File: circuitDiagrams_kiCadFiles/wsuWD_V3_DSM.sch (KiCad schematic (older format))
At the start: 54 parts

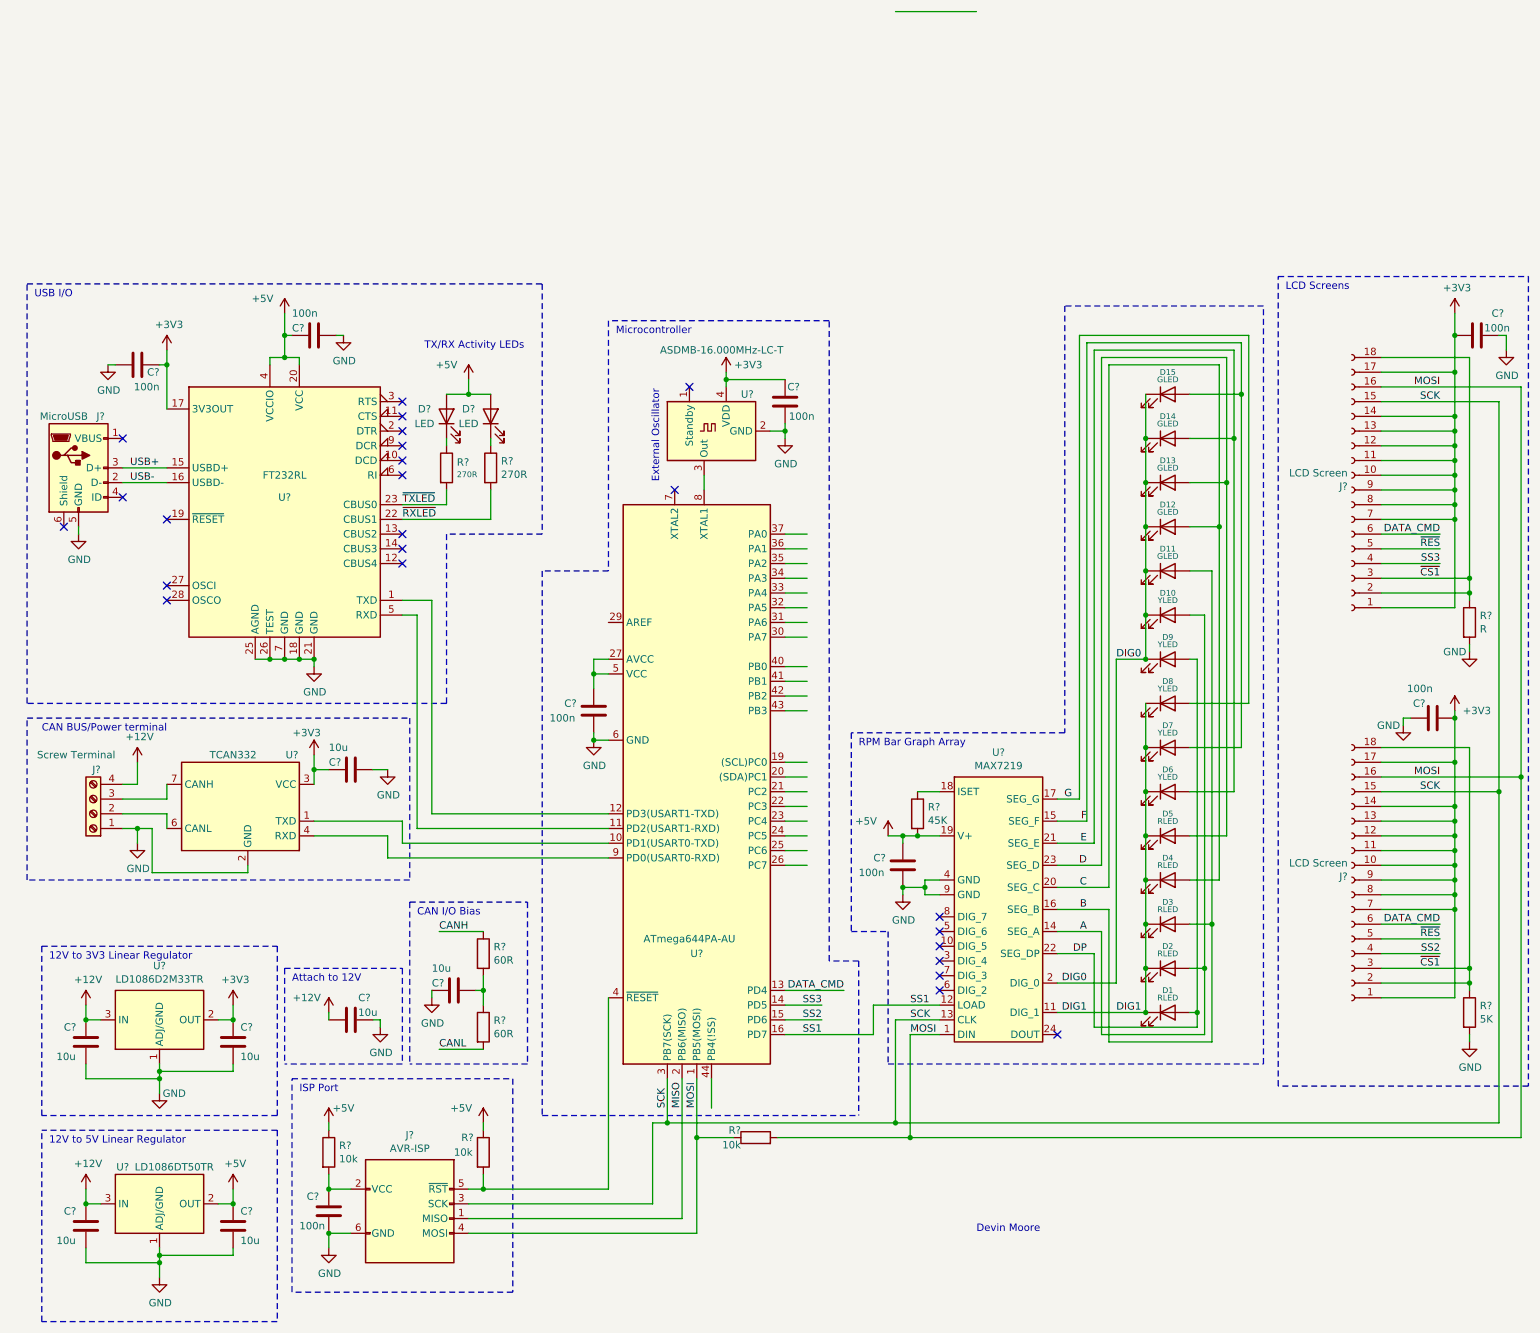
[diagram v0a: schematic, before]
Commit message: Added datasheets and cleaned up schematic
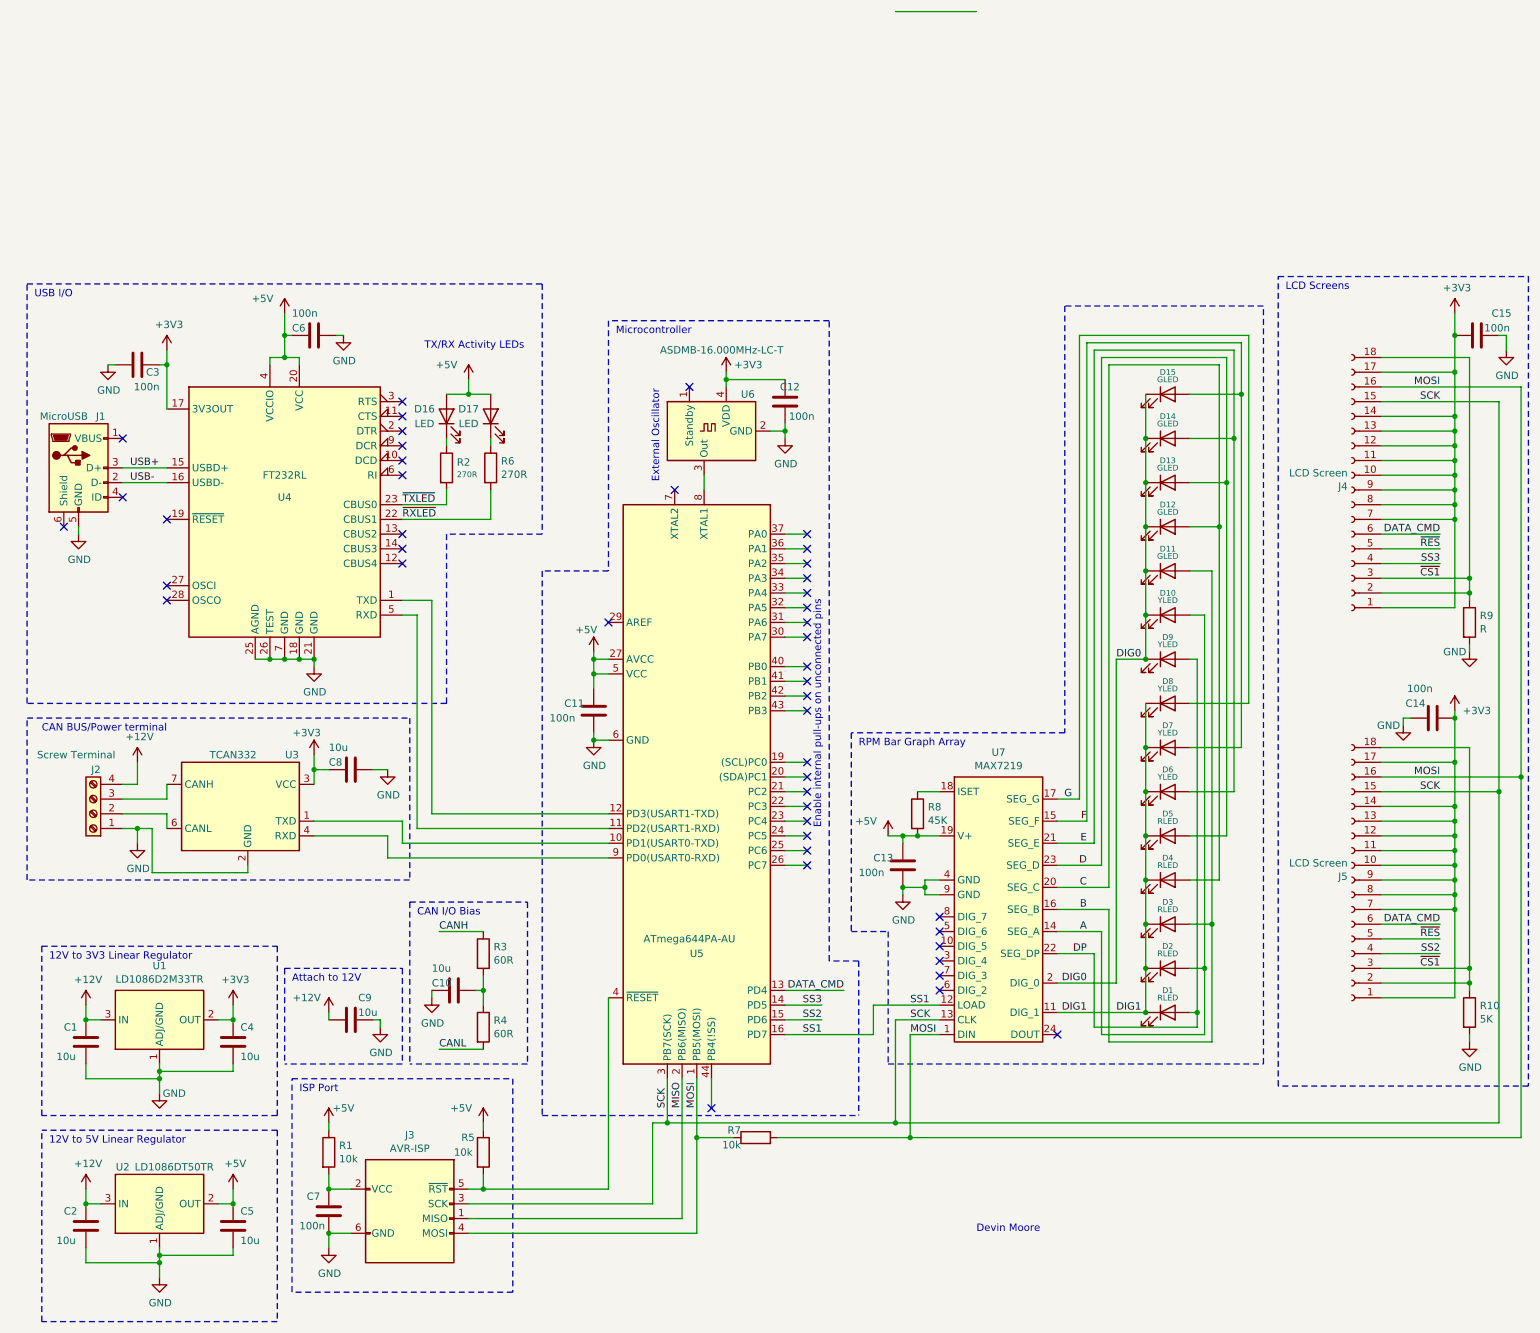
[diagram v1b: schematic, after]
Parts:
- gave numbers to parts that had none: 39
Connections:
- wire segments 313 -> 314
- no-connect marks 24 -> 46
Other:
- note added: "Enable internal pull-ups on unconnected pins"
